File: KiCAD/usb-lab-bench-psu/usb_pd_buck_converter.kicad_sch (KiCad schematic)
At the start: 15 parts, among them U6 LMR16006X

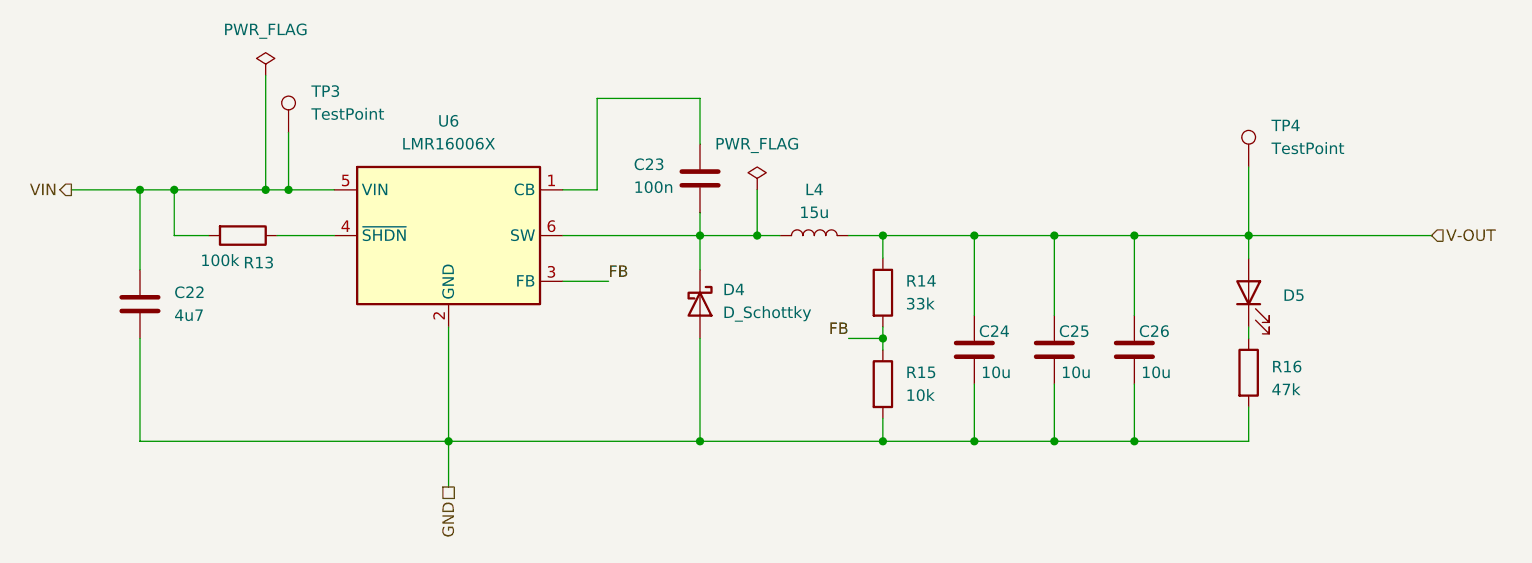
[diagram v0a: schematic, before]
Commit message: Fixed label directions
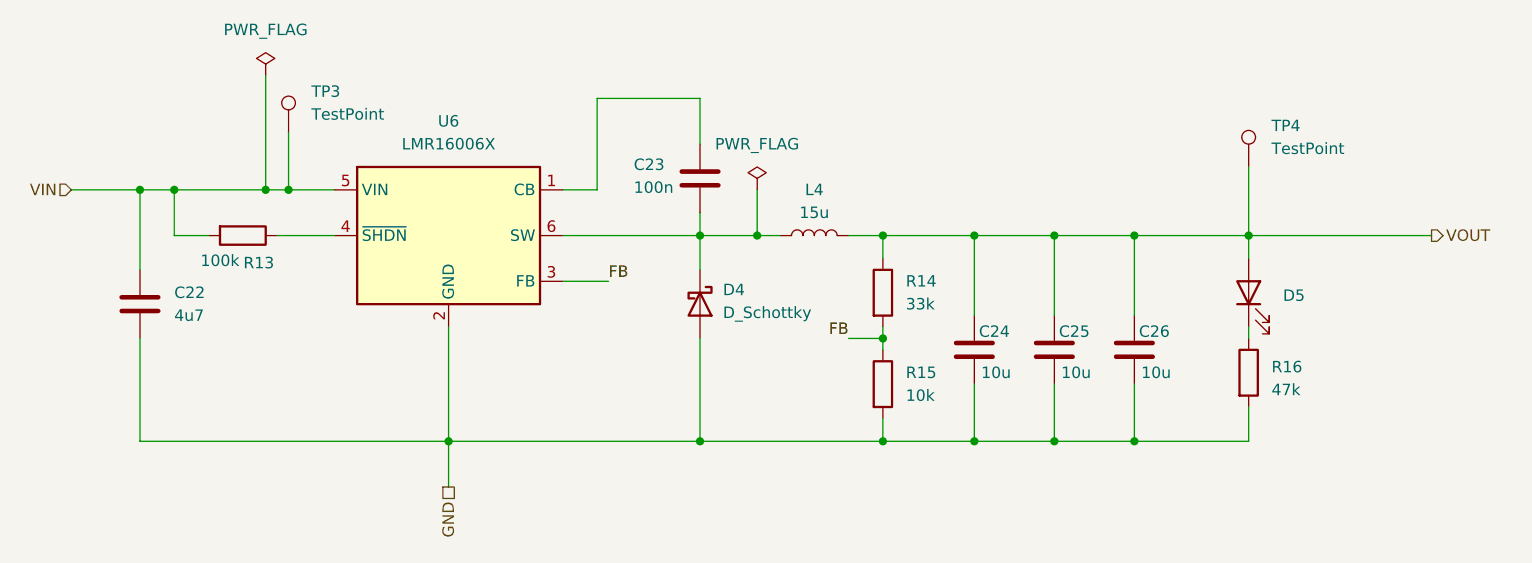
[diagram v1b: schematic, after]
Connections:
- net V-OUT renamed VOUT
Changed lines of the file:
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@@
 		)
 	)
-	(hierarchical_label "V-OUT"
-		(shape input)
+	(hierarchical_label "VOUT"
+		(shape output)
 		(at 210.82 76.2 0)
 		(effects
@@
 	)
 	(hierarchical_label "VIN"
-		(shape output)
+		(shape input)
 		(at 59.69 71.12 180)
 		(effects
@@
 		(instances
 			(project "usb-lab-bench-psu"
-				(path "/63928bc9-e618-488a-a687-c6d5597f31d9/a793a91b-724b-4226-ba64-0dd946e3992c/ac711039-2592-4309-8412-c7dd8d2aeb8d"
-					(reference "C?")
-					(unit 1)
-				)
 				(path "/63928bc9-e618-488a-a687-c6d5597f31d9/cc314cc1-26b0-4e6c-b14c-ea7785b99358/be63a1fd-c574-4431-a13c-219279271461"
 					(reference "C24")
@@
 		(instances
 			(project "usb-lab-bench-psu"
-				(path "/63928bc9-e618-488a-a687-c6d5597f31d9/a793a91b-724b-4226-ba64-0dd946e3992c/ac711039-2592-4309-8412-c7dd8d2aeb8d"
-					(reference "TP?")
-					(unit 1)
-				)
 				(path "/63928bc9-e618-488a-a687-c6d5597f31d9/cc314cc1-26b0-4e6c-b14c-ea7785b99358/be63a1fd-c574-4431-a13c-219279271461"
 					(reference "TP3")
@@
 		(instances
 			(project "usb-lab-bench-psu"
-				(path "/63928bc9-e618-488a-a687-c6d5597f31d9/a793a91b-724b-4226-ba64-0dd946e3992c/ac711039-2592-4309-8412-c7dd8d2aeb8d"
-					(reference "C?")
-					(unit 1)
-				)
 				(path "/63928bc9-e618-488a-a687-c6d5597f31d9/cc314cc1-26b0-4e6c-b14c-ea7785b99358/be63a1fd-c574-4431-a13c-219279271461"
 					(reference "C23")
@@
 		(instances
 			(project "usb-lab-bench-psu"
-				(path "/63928bc9-e618-488a-a687-c6d5597f31d9/a793a91b-724b-4226-ba64-0dd946e3992c/ac711039-2592-4309-8412-c7dd8d2aeb8d"
-					(reference "C?")
-					(unit 1)
-				)
 				(path "/63928bc9-e618-488a-a687-c6d5597f31d9/cc314cc1-26b0-4e6c-b14c-ea7785b99358/be63a1fd-c574-4431-a13c-219279271461"
 					(reference "C25")
@@
 		(instances
 			(project "usb-lab-bench-psu"
-				(path "/63928bc9-e618-488a-a687-c6d5597f31d9/a793a91b-724b-4226-ba64-0dd946e3992c/ac711039-2592-4309-8412-c7dd8d2aeb8d"
-					(reference "R?")
-					(unit 1)
-				)
 				(path "/63928bc9-e618-488a-a687-c6d5597f31d9/cc314cc1-26b0-4e6c-b14c-ea7785b99358/be63a1fd-c574-4431-a13c-219279271461"
 					(reference "R14")
@@
 		(instances
 			(project "usb-lab-bench-psu"
-				(path "/63928bc9-e618-488a-a687-c6d5597f31d9/a793a91b-724b-4226-ba64-0dd946e3992c/ac711039-2592-4309-8412-c7dd8d2aeb8d"
-					(reference "D?")
-					(unit 1)
-				)
 				(path "/63928bc9-e618-488a-a687-c6d5597f31d9/cc314cc1-26b0-4e6c-b14c-ea7785b99358/be63a1fd-c574-4431-a13c-219279271461"
 					(reference "D4")
@@
 		(instances
 			(project "usb-lab-bench-psu"
-				(path "/63928bc9-e618-488a-a687-c6d5597f31d9/a793a91b-724b-4226-ba64-0dd946e3992c/ac711039-2592-4309-8412-c7dd8d2aeb8d"
-					(reference "D?")
-					(unit 1)
-				)
 				(path "/63928bc9-e618-488a-a687-c6d5597f31d9/cc314cc1-26b0-4e6c-b14c-ea7785b99358/be63a1fd-c574-4431-a13c-219279271461"
 					(reference "D5")
@@
 		(instances
 			(project "usb-lab-bench-psu"
-				(path "/63928bc9-e618-488a-a687-c6d5597f31d9/a793a91b-724b-4226-ba64-0dd946e3992c/ac711039-2592-4309-8412-c7dd8d2aeb8d"
-					(reference "L?")
-					(unit 1)
-				)
 				(path "/63928bc9-e618-488a-a687-c6d5597f31d9/cc314cc1-26b0-4e6c-b14c-ea7785b99358/be63a1fd-c574-4431-a13c-219279271461"
 					(reference "L4")
@@
 		(instances
 			(project "usb-lab-bench-psu"
-				(path "/63928bc9-e618-488a-a687-c6d5597f31d9/a793a91b-724b-4226-ba64-0dd946e3992c/ac711039-2592-4309-8412-c7dd8d2aeb8d"
-					(reference "U?")
-					(unit 1)
-				)
 				(path "/63928bc9-e618-488a-a687-c6d5597f31d9/cc314cc1-26b0-4e6c-b14c-ea7785b99358/be63a1fd-c574-4431-a13c-219279271461"
 					(reference "U6")
@@
 		(instances
 			(project "usb-lab-bench-psu"
-				(path "/63928bc9-e618-488a-a687-c6d5597f31d9/a793a91b-724b-4226-ba64-0dd946e3992c/ac711039-2592-4309-8412-c7dd8d2aeb8d"
-					(reference "#FLG?")
-					(unit 1)
-				)
 				(path "/63928bc9-e618-488a-a687-c6d5597f31d9/cc314cc1-26b0-4e6c-b14c-ea7785b99358/be63a1fd-c574-4431-a13c-219279271461"
 					(reference "#FLG06")
@@
 		(instances
 			(project "usb-lab-bench-psu"
-				(path "/63928bc9-e618-488a-a687-c6d5597f31d9/a793a91b-724b-4226-ba64-0dd946e3992c/ac711039-2592-4309-8412-c7dd8d2aeb8d"
-					(reference "C?")
-					(unit 1)
-				)
 				(path "/63928bc9-e618-488a-a687-c6d5597f31d9/cc314cc1-26b0-4e6c-b14c-ea7785b99358/be63a1fd-c574-4431-a13c-219279271461"
 					(reference "C26")
@@
 		(instances
 			(project "usb-lab-bench-psu"
-				(path "/63928bc9-e618-488a-a687-c6d5597f31d9/a793a91b-724b-4226-ba64-0dd946e3992c/ac711039-2592-4309-8412-c7dd8d2aeb8d"
-					(reference "R?")
-					(unit 1)
-				)
 				(path "/63928bc9-e618-488a-a687-c6d5597f31d9/cc314cc1-26b0-4e6c-b14c-ea7785b99358/be63a1fd-c574-4431-a13c-219279271461"
 					(reference "R16")
@@
 		(instances
 			(project "usb-lab-bench-psu"
-				(path "/63928bc9-e618-488a-a687-c6d5597f31d9/a793a91b-724b-4226-ba64-0dd946e3992c/ac711039-2592-4309-8412-c7dd8d2aeb8d"
-					(reference "#FLG?")
-					(unit 1)
-				)
 				(path "/63928bc9-e618-488a-a687-c6d5597f31d9/cc314cc1-26b0-4e6c-b14c-ea7785b99358/be63a1fd-c574-4431-a13c-219279271461"
 					(reference "#FLG05")
@@
 		(instances
 			(project "usb-lab-bench-psu"
-				(path "/63928bc9-e618-488a-a687-c6d5597f31d9/a793a91b-724b-4226-ba64-0dd946e3992c/ac711039-2592-4309-8412-c7dd8d2aeb8d"
-					(reference "TP?")
-					(unit 1)
-				)
 				(path "/63928bc9-e618-488a-a687-c6d5597f31d9/cc314cc1-26b0-4e6c-b14c-ea7785b99358/be63a1fd-c574-4431-a13c-219279271461"
 					(reference "TP4")
@@
 		(instances
 			(project "usb-lab-bench-psu"
-				(path "/63928bc9-e618-488a-a687-c6d5597f31d9/a793a91b-724b-4226-ba64-0dd946e3992c/ac711039-2592-4309-8412-c7dd8d2aeb8d"
-					(reference "C?")
-					(unit 1)
-				)
 				(path "/63928bc9-e618-488a-a687-c6d5597f31d9/cc314cc1-26b0-4e6c-b14c-ea7785b99358/be63a1fd-c574-4431-a13c-219279271461"
 					(reference "C22")
@@
 		(instances
 			(project "usb-lab-bench-psu"
-				(path "/63928bc9-e618-488a-a687-c6d5597f31d9/a793a91b-724b-4226-ba64-0dd946e3992c/ac711039-2592-4309-8412-c7dd8d2aeb8d"
-					(reference "R?")
-					(unit 1)
-				)
 				(path "/63928bc9-e618-488a-a687-c6d5597f31d9/cc314cc1-26b0-4e6c-b14c-ea7785b99358/be63a1fd-c574-4431-a13c-219279271461"
 					(reference "R13")
@@
 		(instances
 			(project "usb-lab-bench-psu"
-				(path "/63928bc9-e618-488a-a687-c6d5597f31d9/a793a91b-724b-4226-ba64-0dd946e3992c/ac711039-2592-4309-8412-c7dd8d2aeb8d"
-					(reference "R?")
-					(unit 1)
-				)
 				(path "/63928bc9-e618-488a-a687-c6d5597f31d9/cc314cc1-26b0-4e6c-b14c-ea7785b99358/be63a1fd-c574-4431-a13c-219279271461"
 					(reference "R15")

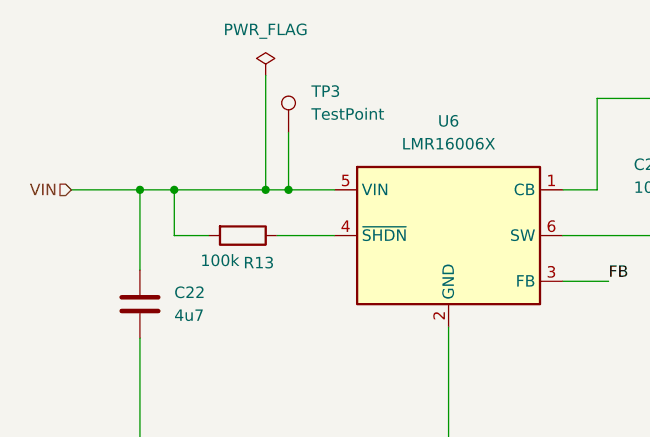
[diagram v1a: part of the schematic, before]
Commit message: tweaked design of current limiter, added GPIO expander to USB-PD circuit
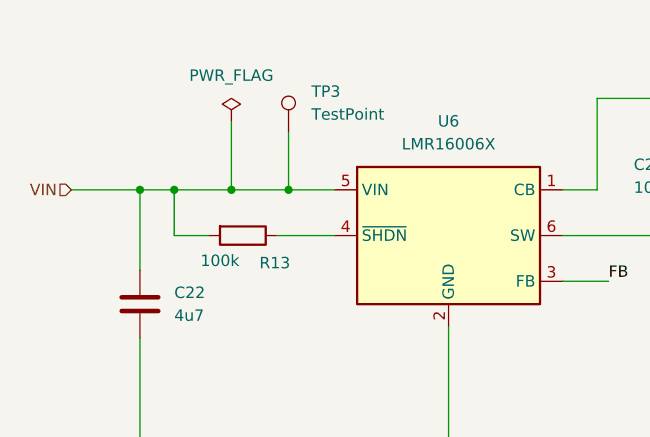
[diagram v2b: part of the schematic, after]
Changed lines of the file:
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@@
-	)
-	(junction
-		(at 81.28 71.12)
-		(diameter 0)
-		(color 0 0 0 0)
 	)
 	(junction
@@
 	)
 	(junction
+		(at 77.47 71.12)
+		(diameter 0)
+		(color 0 0 0 0)
+	)
+	(junction
 		(at 177.8 76.2)
 		(diameter 0)
@@
 	(wire
 		(pts
-			(xy 81.28 71.12) (xy 83.82 71.12)
-		)
-		(stroke
-			(width 0)
-			(type default)
-		)
-	)
-	(wire
-		(pts
 			(xy 160.02 76.2) (xy 168.91 76.2)
 		)
@@
 	(wire
 		(pts
+			(xy 77.47 71.12) (xy 83.82 71.12)
+		)
+		(stroke
+			(width 0)
+			(type default)
+		)
+	)
+	(wire
+		(pts
 			(xy 160.02 92.71) (xy 160.02 99.06)
 		)
@@
 	(wire
 		(pts
-			(xy 81.28 58.42) (xy 81.28 71.12)
+			(xy 77.47 63.5) (xy 77.47 71.12)
 		)
 		(stroke
@@
 	(wire
 		(pts
-			(xy 71.12 71.12) (xy 81.28 71.12)
+			(xy 71.12 71.12) (xy 77.47 71.12)
 		)
 		(stroke
@@
 	(symbol
 		(lib_id "power:PWR_FLAG")
-		(at 81.28 58.42 0)
+		(at 77.47 63.5 0)
 		(unit 1)
 		(exclude_from_sim no)
@@
 		(fields_autoplaced yes)
 		(property "Reference" "#FLG05"
-			(at 81.28 56.515 0)
+			(at 77.47 61.595 0)
 			(effects
 				(font
@@
 		)
 		(property "Value" "PWR_FLAG"
-			(at 81.28 53.34 0)
+			(at 77.47 58.42 0)
 			(effects
 				(font
@@
 		)
 		(property "Footprint" ""
-			(at 81.28 58.42 0)
+			(at 77.47 63.5 0)
 			(effects
 				(font
@@
 		)
 		(property "Datasheet" "~"
-			(at 81.28 58.42 0)
+			(at 77.47 63.5 0)
 			(effects
 				(font
@@
 		)
 		(property "Description" "Special symbol for telling ERC where power comes from"
-			(at 81.28 58.42 0)
+			(at 77.47 63.5 0)
 			(effects
 				(font
@@
 		(dnp no)
 		(property "Reference" "R13"
-			(at 80.518 79.248 90)
-			(effects
-				(font
+			(at 82.296 79.248 90)
+			(effects
+				(font
